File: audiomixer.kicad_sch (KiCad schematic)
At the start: 0 parts

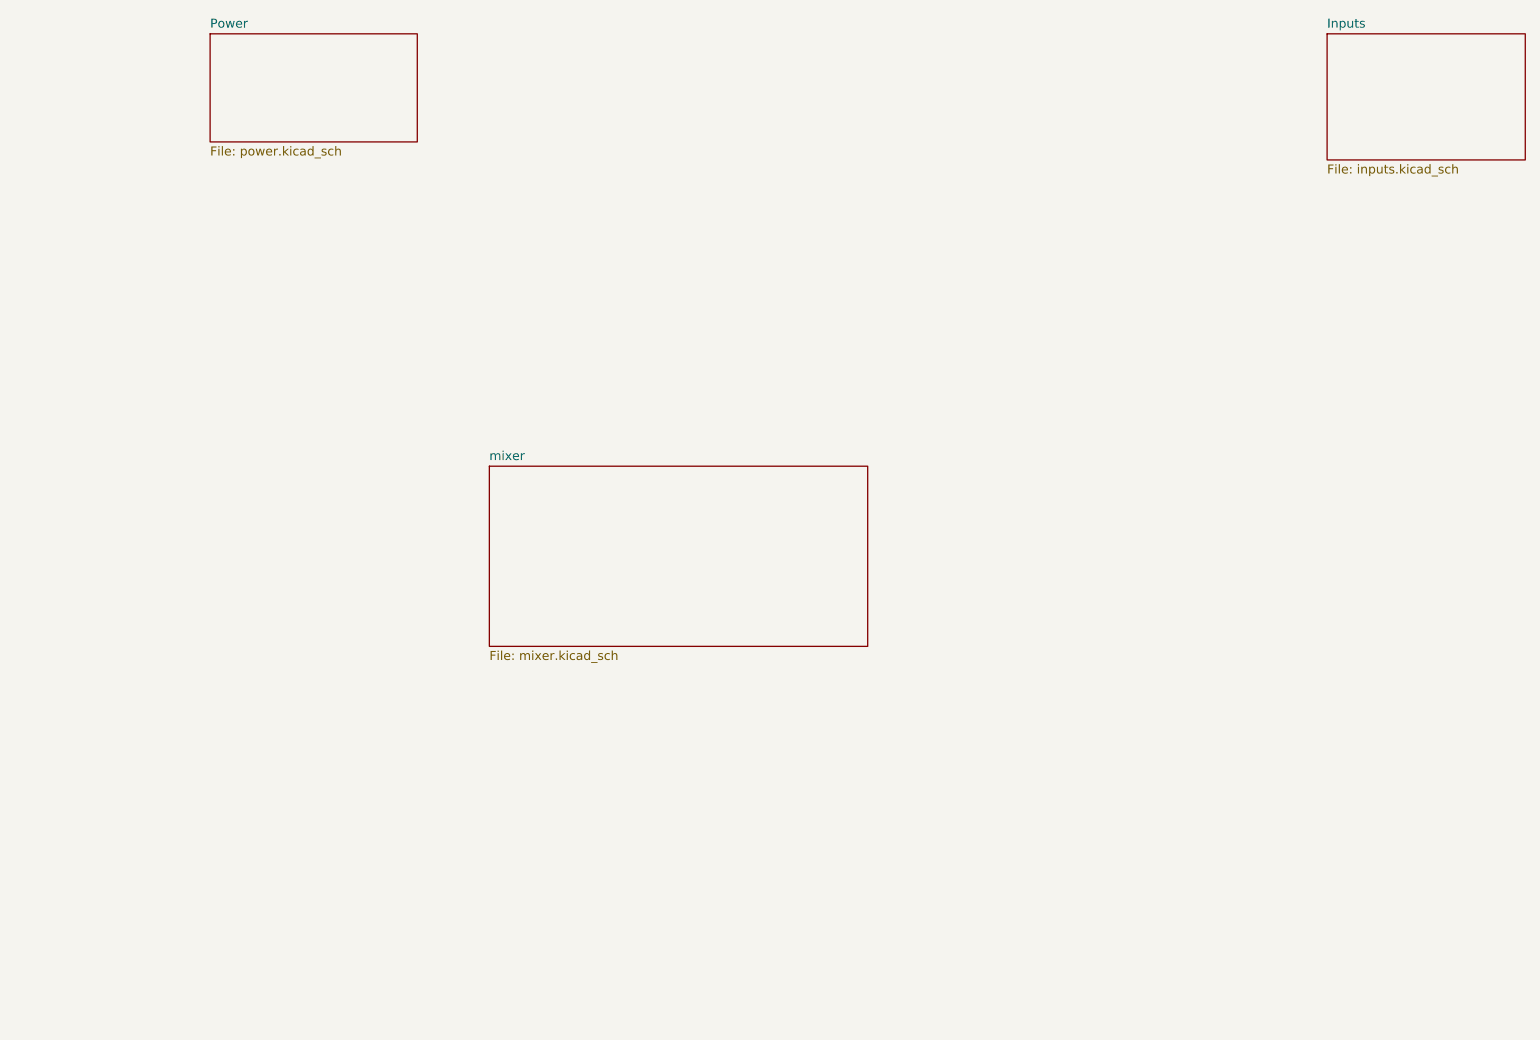
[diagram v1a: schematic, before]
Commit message: Refactored and made modular inputs
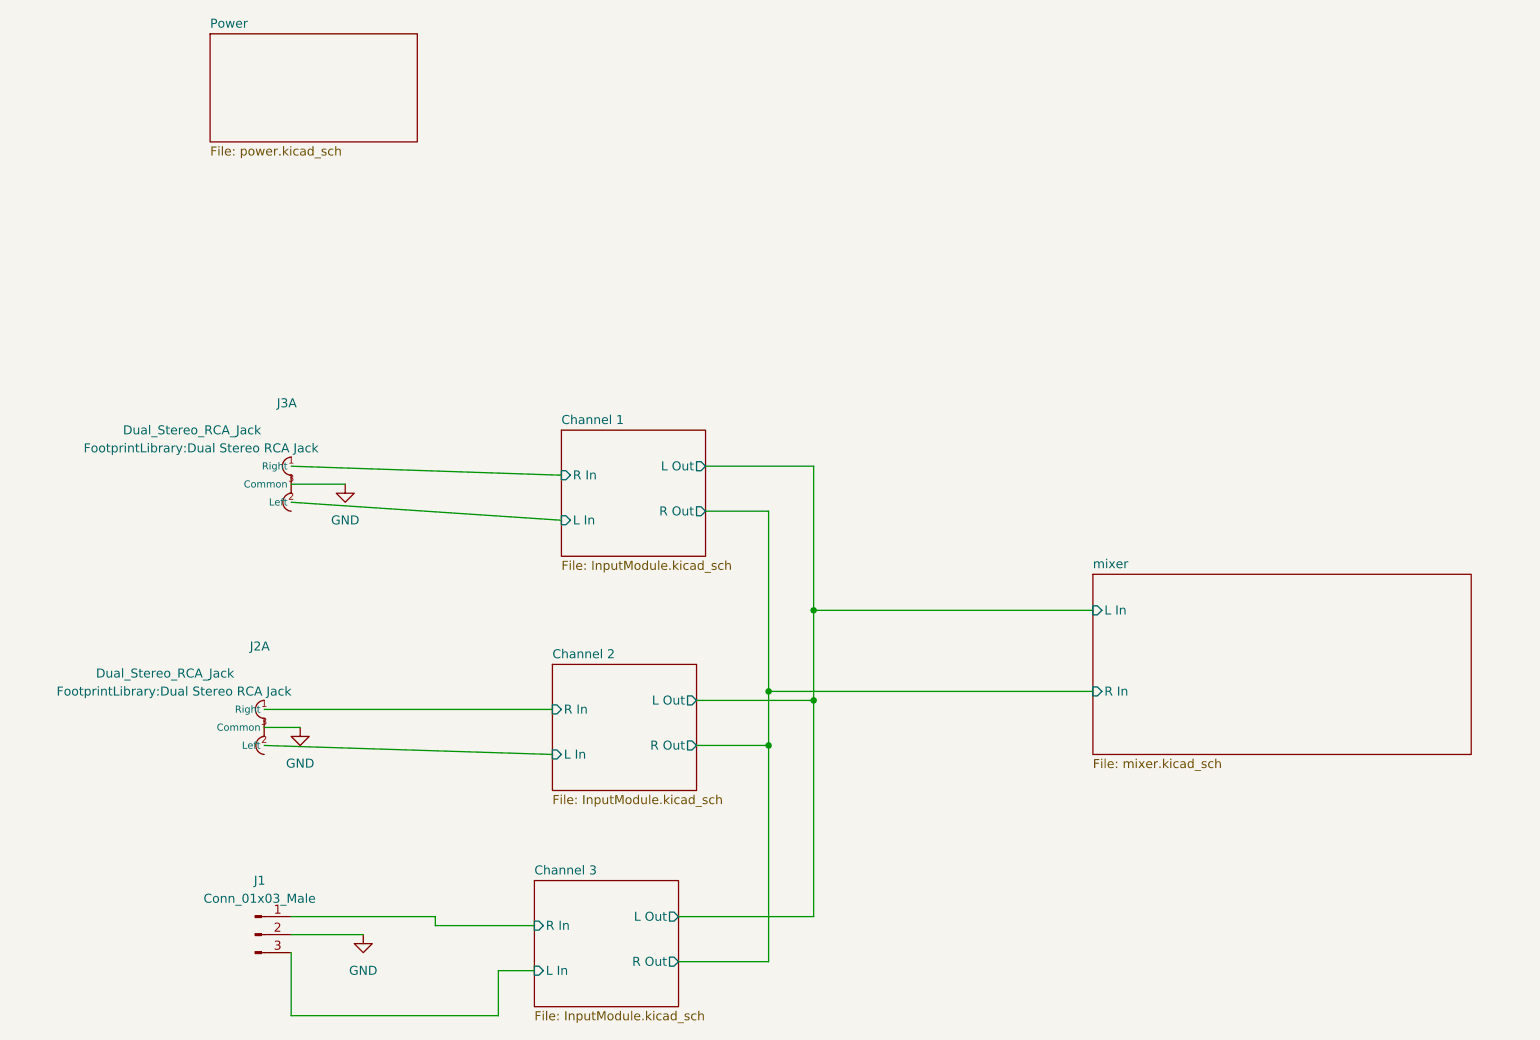
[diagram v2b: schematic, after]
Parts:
- added J1: Conn_01x03_Male, symbol Connector:Conn_01x03_Male
- added J2, J3: Dual_Stereo_RCA_Jack, FootprintLibrary:Dual Stereo RCA Jack, symbol CustomComponentLibrary:Dual_Stereo_RCA_Jack
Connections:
- new net Channel 1/L In: J3.2 (Left)
- new net Channel 1/R In: J3.1 (Right)
- new net Channel 2/L In: J2.2 (Left)
- new net Channel 2/R In: J2.1 (Right)
- new net Channel 3/L In: J1.3 (Pin_3)
- new net Channel 3/R In: J1.1 (Pin_1)
- new net GND: J1.2 (Pin_2), J2.3 (Common), J3.3 (Common)
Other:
- removed sheet Inputs
- added sheet Channel 1 (InputModule.kicad_sch)
- added sheet Channel 2 (InputModule.kicad_sch)
- added sheet Channel 3 (InputModule.kicad_sch)
- sheet mixer ports: added L In, R In; removed none

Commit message: Update footprints
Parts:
- J1: value Conn_01x03_Male -> Channel 3 In

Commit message: Finalize schematic and start with PCB layout
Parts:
- removed J3: Dual_Stereo_RCA_Jack, FootprintLibrary:Dual Stereo RCA Jack, symbol CustomComponentLibrary:Dual_Stereo_RCA_Jack
- added unit 2 of J2
- J1: footprint (none) -> Connector_JST:JST_XA_B03B-XASK-1_1x03_P2.50mm_Vertical
- J2: footprint FootprintLibrary:Dual Stereo RCA Jack -> CustomFootprintLibrary:Dual Stereo RCA Jack
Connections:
- net Channel 1/L In: now also J2.2 (Left)
- net Channel 1/R In: now also J2.1 (Right)
- net Channel 2/L In: now also J2.5 (Left); no longer J2.2 (Left)
- net Channel 2/R In: now also J2.4 (Right); no longer J2.1 (Right)
- net GND: now also J2.6 (Common)
